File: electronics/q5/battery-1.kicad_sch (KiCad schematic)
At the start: 6 parts, among them Q1 Discharge FET, Q2 Charge FET

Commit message: Q5 design lock: JLC Basic substitutions, re-verified board, cost estimator
Co-Authored-By: Claude Opus 5.5 <noreply@anthropic.com>
Claude-Session: https://claude.ai/code/session_01UrkzLMrBi6iLPSL5SbMCA7
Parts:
- C4: MPN GRM188R71H104KA93D -> CC0603KRX7R9BB104
- R7: MPN RC0603FR-07330RL -> 0603WAF3300T5E
- R8: MPN RC0603FR-072K2L -> 0603WAF2201T5E
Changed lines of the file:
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@@
       (in_bom yes) (on_board yes) (dnp no)
  (property "Reference" "C4" (at 294.64 73.66 0) (effects (font (size 1.524 1.524)))) (property "Value" "100n" (at 294.64 77.46999999999998 0) (effects (font (size 1.524 1.524))))
-      (property "Footprint" "CountFidgetQ5:Capacitor_SMD_C_0603_1608Metric" (at 294.64 82.55 0) (effects (font (size 1.27 1.27)) (hide yes))) (property "MPN" "GRM188R71H104KA93D" (at 294.64 77.46999999999998 0) (effects (font (size 1.524 1.524)) (hide yes)))
+      (property "Footprint" "CountFidgetQ5:Capacitor_SMD_C_0603_1608Metric" (at 294.64 82.55 0) (effects (font (size 1.27 1.27)) (hide yes))) (property "MPN" "CC0603KRX7R9BB104" (at 294.64 77.46999999999998 0) (effects (font (size 1.524 1.524)) (hide yes)))
       (property "Description" "100 nF, 50 V, X7R" (at 294.64 82.55 0) (effects (font (size 1.27 1.27)) (hide yes)))
       (pin "1")(pin "2")
@@
       (in_bom yes) (on_board yes) (dnp no)
  (property "Reference" "R7" (at 105.41 229.87 0) (effects (font (size 1.524 1.524)))) (property "Value" "330" (at 105.41 233.68 0) (effects (font (size 1.524 1.524))))
-      (property "Footprint" "CountFidgetQ5:Resistor_SMD_R_0603_1608Metric" (at 105.41 238.76 0) (effects (font (size 1.27 1.27)) (hide yes))) (property "MPN" "RC0603FR-07330RL" (at 105.41 233.68 0) (effects (font (size 1.524 1.524)) (hide yes)))
+      (property "Footprint" "CountFidgetQ5:Resistor_SMD_R_0603_1608Metric" (at 105.41 238.76 0) (effects (font (size 1.27 1.27)) (hide yes))) (property "MPN" "0603WAF3300T5E" (at 105.41 233.68 0) (effects (font (size 1.524 1.524)) (hide yes)))
       (property "Description" "1%, 0603, 0.1 W" (at 105.41 238.76 0) (effects (font (size 1.27 1.27)) (hide yes)))
       (pin "1")(pin "2")
@@
       (in_bom yes) (on_board yes) (dnp no)
  (property "Reference" "R8" (at 294.64 229.87 0) (effects (font (size 1.524 1.524)))) (property "Value" "2.2k" (at 294.64 233.68 0) (effects (font (size 1.524 1.524))))
-      (property "Footprint" "CountFidgetQ5:Resistor_SMD_R_0603_1608Metric" (at 294.64 238.76 0) (effects (font (size 1.27 1.27)) (hide yes))) (property "MPN" "RC0603FR-072K2L" (at 294.64 233.68 0) (effects (font (size 1.524 1.524)) (hide yes)))
+      (property "Footprint" "CountFidgetQ5:Resistor_SMD_R_0603_1608Metric" (at 294.64 238.76 0) (effects (font (size 1.27 1.27)) (hide yes))) (property "MPN" "0603WAF2201T5E" (at 294.64 233.68 0) (effects (font (size 1.524 1.524)) (hide yes)))
       (property "Description" "1%, 0603, 0.1 W" (at 294.64 238.76 0) (effects (font (size 1.27 1.27)) (hide yes)))
       (pin "1")(pin "2")

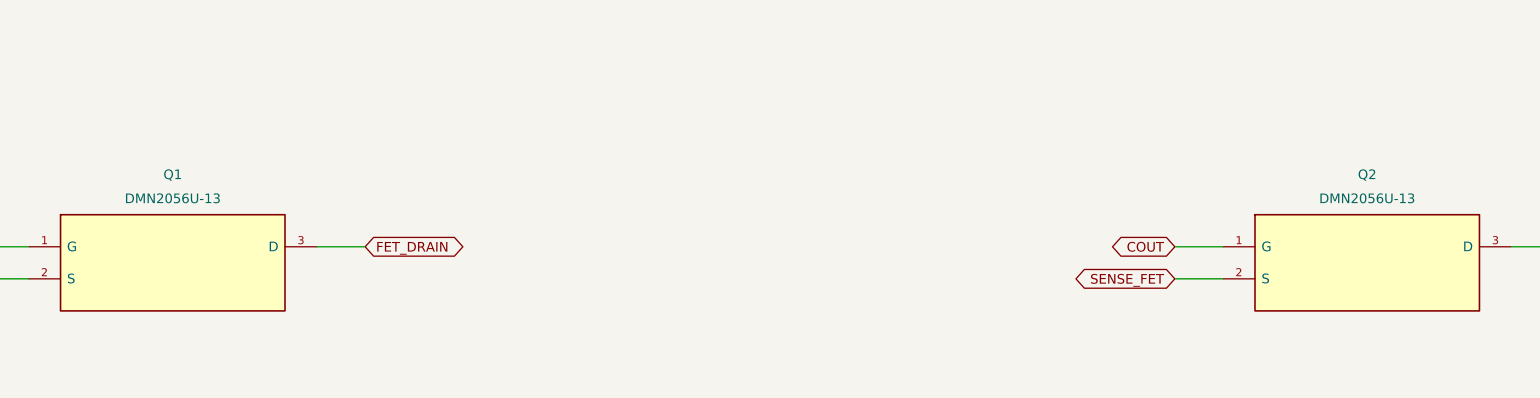
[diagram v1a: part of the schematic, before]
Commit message: Move nine part types to JLC Basic; 16 Extended types remain, each justified
R4 18k (16.7 mA charge), temperature window 56k/82k/18k/12k (7.26-35.83 C),
R32 75 ohm, Q1/Q2 AO3400A, 2.2 uF and 10 uF 50 V 0805 capacitors. Fresh
ERC/DRC/parity on unchanged routing, stock 42/42, exports, JLC footprint
fit and pin names, power/latch checks re-run. About $28 less per order.

Co-Authored-By: Claude Opus 5.5 <noreply@anthropic.com>
Claude-Session: https://claude.ai/code/session_01UrkzLMrBi6iLPSL5SbMCA7
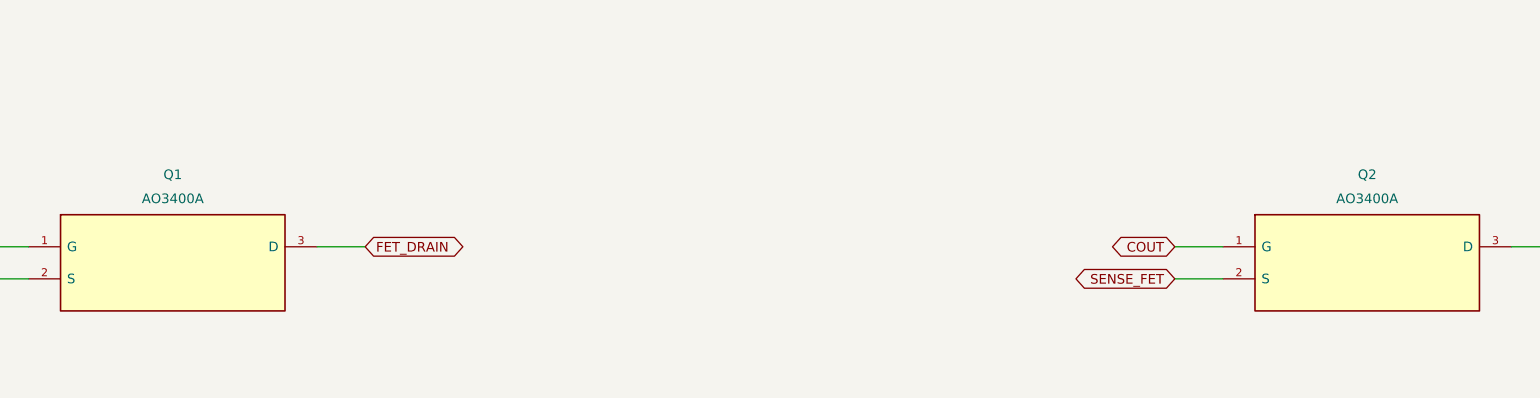
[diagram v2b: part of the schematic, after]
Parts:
- Q1, Q2: MPN DMN2056U-13 -> AO3400A
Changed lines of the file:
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@@
       (in_bom yes) (on_board yes) (dnp no)
  (property "Reference" "Q1" (at 105.41 147.32 0) (effects (font (size 1.524 1.524)))) (property "Value" "Discharge FET" (at 105.41 151.13 0) (effects (font (size 1.524 1.524)) (hide yes)))
-      (property "Footprint" "CountFidgetQ5:Package_TO_SOT_SMD_SOT-23" (at 105.41 161.29 0) (effects (font (size 1.27 1.27)) (hide yes))) (property "MPN" "DMN2056U-13" (at 105.41 151.13 0) (effects (font (size 1.524 1.524))))
-      (property "Description" "; exact same-device reel suffix -13; no electrical polarity change" (at 105.41 161.29 0) (effects (font (size 1.27 1.27)) (hide yes)))
+      (property "Footprint" "CountFidgetQ5:Package_TO_SOT_SMD_SOT-23" (at 105.41 161.29 0) (effects (font (size 1.27 1.27)) (hide yes))) (property "MPN" "AO3400A" (at 105.41 151.13 0) (effects (font (size 1.524 1.524))))
+      (property "Description" "AO3400A: SOT-23 1 G / 2 S / 3 D, 30 V, 48 mOhm max at VGS 2.5 V; BQ29700 FET per TI Fig. 9-1" (at 105.41 161.29 0) (effects (font (size 1.27 1.27)) (hide yes)))
       (pin "1")(pin "2")(pin "3")
       (instances (project "click-counter-Q5" (path "/7c190cd8-3ca2-5363-8a92-396d30a08243/a2b4a664-6944-5f42-8858-eb265e415837" (reference "Q1") (unit 1)))))
@@
       (in_bom yes) (on_board yes) (dnp no)
  (property "Reference" "Q2" (at 294.64 147.32 0) (effects (font (size 1.524 1.524)))) (property "Value" "Charge FET" (at 294.64 151.13 0) (effects (font (size 1.524 1.524)) (hide yes)))
-      (property "Footprint" "CountFidgetQ5:Package_TO_SOT_SMD_SOT-23" (at 294.64 161.29 0) (effects (font (size 1.27 1.27)) (hide yes))) (property "MPN" "DMN2056U-13" (at 294.64 151.13 0) (effects (font (size 1.524 1.524))))
-      (property "Description" "; exact same-device reel suffix -13; no electrical polarity change" (at 294.64 161.29 0) (effects (font (size 1.27 1.27)) (hide yes)))
+      (property "Footprint" "CountFidgetQ5:Package_TO_SOT_SMD_SOT-23" (at 294.64 161.29 0) (effects (font (size 1.27 1.27)) (hide yes))) (property "MPN" "AO3400A" (at 294.64 151.13 0) (effects (font (size 1.524 1.524))))
+      (property "Description" "AO3400A: SOT-23 1 G / 2 S / 3 D, 30 V, 48 mOhm max at VGS 2.5 V; BQ29700 FET per TI Fig. 9-1" (at 294.64 161.29 0) (effects (font (size 1.27 1.27)) (hide yes)))
       (pin "1")(pin "2")(pin "3")
       (instances (project "click-counter-Q5" (path "/7c190cd8-3ca2-5363-8a92-396d30a08243/a2b4a664-6944-5f42-8858-eb265e415837" (reference "Q2") (unit 1)))))
